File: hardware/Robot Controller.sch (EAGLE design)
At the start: 18 parts

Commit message: tighten up PCB
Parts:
- removed S1: (no value), switch-omron:10-XX
- added JP7: (no value), pinhead:PINHD-1X8
- JP8: device pinhead:PINHD-1X10 -> pinhead:PINHD-1X2
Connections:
- net GND: now also JP8.2; no longer JP8.10, S1.S1
- net N$23: now also JP7.8; no longer JP8.8
- net N$24: now also JP7.7; no longer JP8.7
- net N$25: now also JP7.6; no longer JP8.6
- net N$26: now also JP7.5; no longer JP8.5
- net N$27: now also JP7.4; no longer JP8.4
- net N$28: now also JP7.1; no longer JP8.1
- net N$29: now also JP7.2; no longer JP8.2
- net N$30: now also JP7.3; no longer JP8.3
- net N$31: now also JP8.1; no longer S1.P
- net VCC: no longer JP8.9
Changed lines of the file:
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@@
 <part name="SUPPLY4" library="SparkFun-Aesthetics" deviceset="VCC" device=""/>
 <part name="JP6" library="pinhead" deviceset="PINHD-1X3" device=""/>
-<part name="JP8" library="pinhead" deviceset="PINHD-1X10" device=""/>
-<part name="SUPPLY5" library="SparkFun-Aesthetics" deviceset="VCC" device=""/>
-<part name="GND11" library="SparkFun-Aesthetics" deviceset="GND" device=""/>
-<part name="S1" library="switch-omron" deviceset="10-XX" device=""/>
 <part name="GND12" library="SparkFun-Aesthetics" deviceset="GND" device=""/>
+<part name="JP7" library="pinhead" deviceset="PINHD-1X8" device=""/>
+<part name="JP8" library="pinhead" deviceset="PINHD-1X2" device=""/>
 </parts>
 <sheets>
@@
 <instance part="SUPPLY4" gate="1" x="121.92" y="86.36" rot="R180"/>
 <instance part="JP6" gate="A" x="38.1" y="91.44"/>
-<instance part="JP8" gate="A" x="5.08" y="104.14" rot="R90"/>
-<instance part="SUPPLY5" gate="1" x="15.24" y="96.52" rot="R180"/>
-<instance part="GND11" gate="1" x="17.78" y="91.44"/>
-<instance part="S1" gate="1" x="63.5" y="124.46" rot="R270"/>
-<instance part="GND12" gate="1" x="73.66" y="121.92" rot="R90"/>
+<instance part="GND12" gate="1" x="73.66" y="124.46" rot="R90"/>
+<instance part="JP7" gate="A" x="5.08" y="104.14" rot="R90"/>
+<instance part="JP8" gate="G$1" x="66.04" y="127" rot="R90"/>
 </instances>
 <busses>
@@
 </segment>
 <segment>
-<pinref part="JP8" gate="A" pin="10"/>
-<pinref part="GND11" gate="1" pin="GND"/>
-<wire x1="17.78" y1="101.6" x2="17.78" y2="93.98" width="0.1524" layer="91"/>
-<junction x="17.78" y="101.6"/>
-<junction x="17.78" y="93.98"/>
-</segment>
-<segment>
-<pinref part="S1" gate="1" pin="S1"/>
 <pinref part="GND12" gate="1" pin="GND"/>
-<wire x1="68.58" y1="121.92" x2="71.12" y2="121.92" width="0.1524" layer="91"/>
-<junction x="68.58" y="121.92"/>
-<junction x="71.12" y="121.92"/>
+<wire x1="66.04" y1="124.46" x2="71.12" y2="124.46" width="0.1524" layer="91"/>
+<junction x="71.12" y="124.46"/>
+<pinref part="JP8" gate="G$1" pin="2"/>
+<junction x="66.04" y="124.46"/>
 </segment>
 </net>
@@
 <junction x="121.92" y="86.36"/>
 <junction x="119.38" y="96.52"/>
-</segment>
-<segment>
-<pinref part="JP8" gate="A" pin="9"/>
-<pinref part="SUPPLY5" gate="1" pin="VCC"/>
-<wire x1="15.24" y1="101.6" x2="15.24" y2="96.52" width="0.1524" layer="91"/>
-<junction x="15.24" y="96.52"/>
-<junction x="15.24" y="101.6"/>
 </segment>
 </net>
@@
 <wire x1="12.7" y1="88.9" x2="35.56" y2="88.9" width="0.1524" layer="91"/>
 <junction x="35.56" y="88.9"/>
-<pinref part="JP8" gate="A" pin="8"/>
 <wire x1="12.7" y1="93.98" x2="12.7" y2="101.6" width="0.1524" layer="91"/>
+<pinref part="JP7" gate="A" pin="8"/>
 <junction x="12.7" y="101.6"/>
 </segment>
@@
 <wire x1="10.16" y1="86.36" x2="10.16" y2="93.98" width="0.1524" layer="91"/>
 <junction x="50.8" y="60.96"/>
-<pinref part="JP8" gate="A" pin="7"/>
 <wire x1="10.16" y1="93.98" x2="10.16" y2="101.6" width="0.1524" layer="91"/>
+<pinref part="JP7" gate="A" pin="7"/>
 <junction x="10.16" y="101.6"/>
 </segment>
@@
 <wire x1="7.62" y1="83.82" x2="7.62" y2="93.98" width="0.1524" layer="91"/>
 <junction x="50.8" y="58.42"/>
-<pinref part="JP8" gate="A" pin="6"/>
 <wire x1="7.62" y1="93.98" x2="7.62" y2="101.6" width="0.1524" layer="91"/>
+<pinref part="JP7" gate="A" pin="6"/>
 <junction x="7.62" y="101.6"/>
 </segment>
@@
 <wire x1="5.08" y1="81.28" x2="5.08" y2="93.98" width="0.1524" layer="91"/>
 <junction x="50.8" y="55.88"/>
-<pinref part="JP8" gate="A" pin="5"/>
 <wire x1="5.08" y1="93.98" x2="5.08" y2="101.6" width="0.1524" layer="91"/>
+<pinref part="JP7" gate="A" pin="5"/>
 <junction x="5.08" y="101.6"/>
 </segment>
@@
 <wire x1="2.54" y1="78.74" x2="2.54" y2="93.98" width="0.1524" layer="91"/>
 <junction x="50.8" y="53.34"/>
-<pinref part="JP8" gate="A" pin="4"/>
 <wire x1="2.54" y1="93.98" x2="2.54" y2="101.6" width="0.1524" layer="91"/>
+<pinref part="JP7" gate="A" pin="4"/>
 <junction x="2.54" y="101.6"/>
 </segment>
@@
 <wire x1="-5.08" y1="86.36" x2="-5.08" y2="93.98" width="0.1524" layer="91"/>
 <junction x="66.04" y="55.88"/>
-<pinref part="JP8" gate="A" pin="1"/>
 <wire x1="-5.08" y1="93.98" x2="-5.08" y2="101.6" width="0.1524" layer="91"/>
+<pinref part="JP7" gate="A" pin="1"/>
 <junction x="-5.08" y="101.6"/>
 </segment>
@@
 <wire x1="-2.54" y1="83.82" x2="-2.54" y2="93.98" width="0.1524" layer="91"/>
 <junction x="66.04" y="53.34"/>
-<pinref part="JP8" gate="A" pin="2"/>
 <wire x1="-2.54" y1="93.98" x2="-2.54" y2="101.6" width="0.1524" layer="91"/>
+<pinref part="JP7" gate="A" pin="2"/>
 <junction x="-2.54" y="101.6"/>
 </segment>
@@
 <wire x1="0" y1="81.28" x2="0" y2="93.98" width="0.1524" layer="91"/>
 <junction x="66.04" y="50.8"/>
-<pinref part="JP8" gate="A" pin="3"/>
 <wire x1="0" y1="93.98" x2="0" y2="101.6" width="0.1524" layer="91"/>
+<pinref part="JP7" gate="A" pin="3"/>
 <junction x="0" y="101.6"/>
 </segment>
@@
 <wire x1="45.72" y1="83.82" x2="48.26" y2="83.82" width="0.1524" layer="91"/>
 <wire x1="48.26" y1="83.82" x2="48.26" y2="124.46" width="0.1524" layer="91"/>
-<pinref part="S1" gate="1" pin="P"/>
-<wire x1="48.26" y1="124.46" x2="58.42" y2="124.46" width="0.1524" layer="91"/>
+<wire x1="48.26" y1="124.46" x2="63.5" y2="124.46" width="0.1524" layer="91"/>
 <junction x="50.8" y="73.66"/>
-<junction x="58.42" y="124.46"/>
-</segment>
-</net>
+<pinref part="JP8" gate="G$1" pin="1"/>
+<junction x="63.5" y="124.46"/>
+</segment>
+</net>

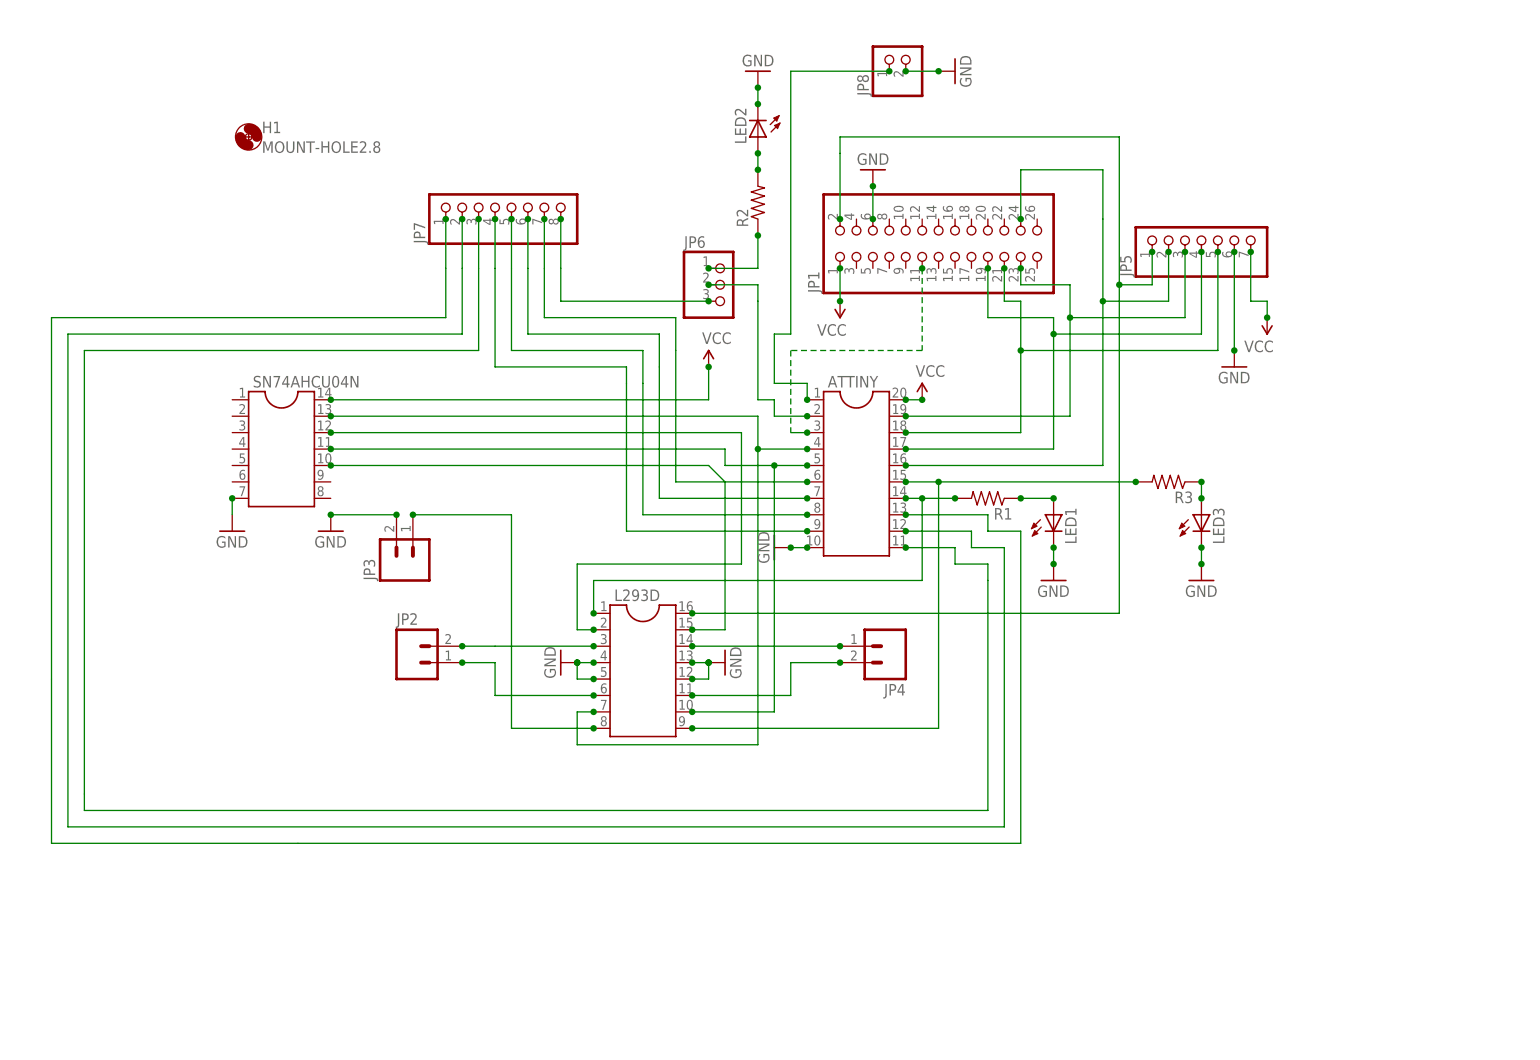
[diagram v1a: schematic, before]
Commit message: working on cleaning up schematic
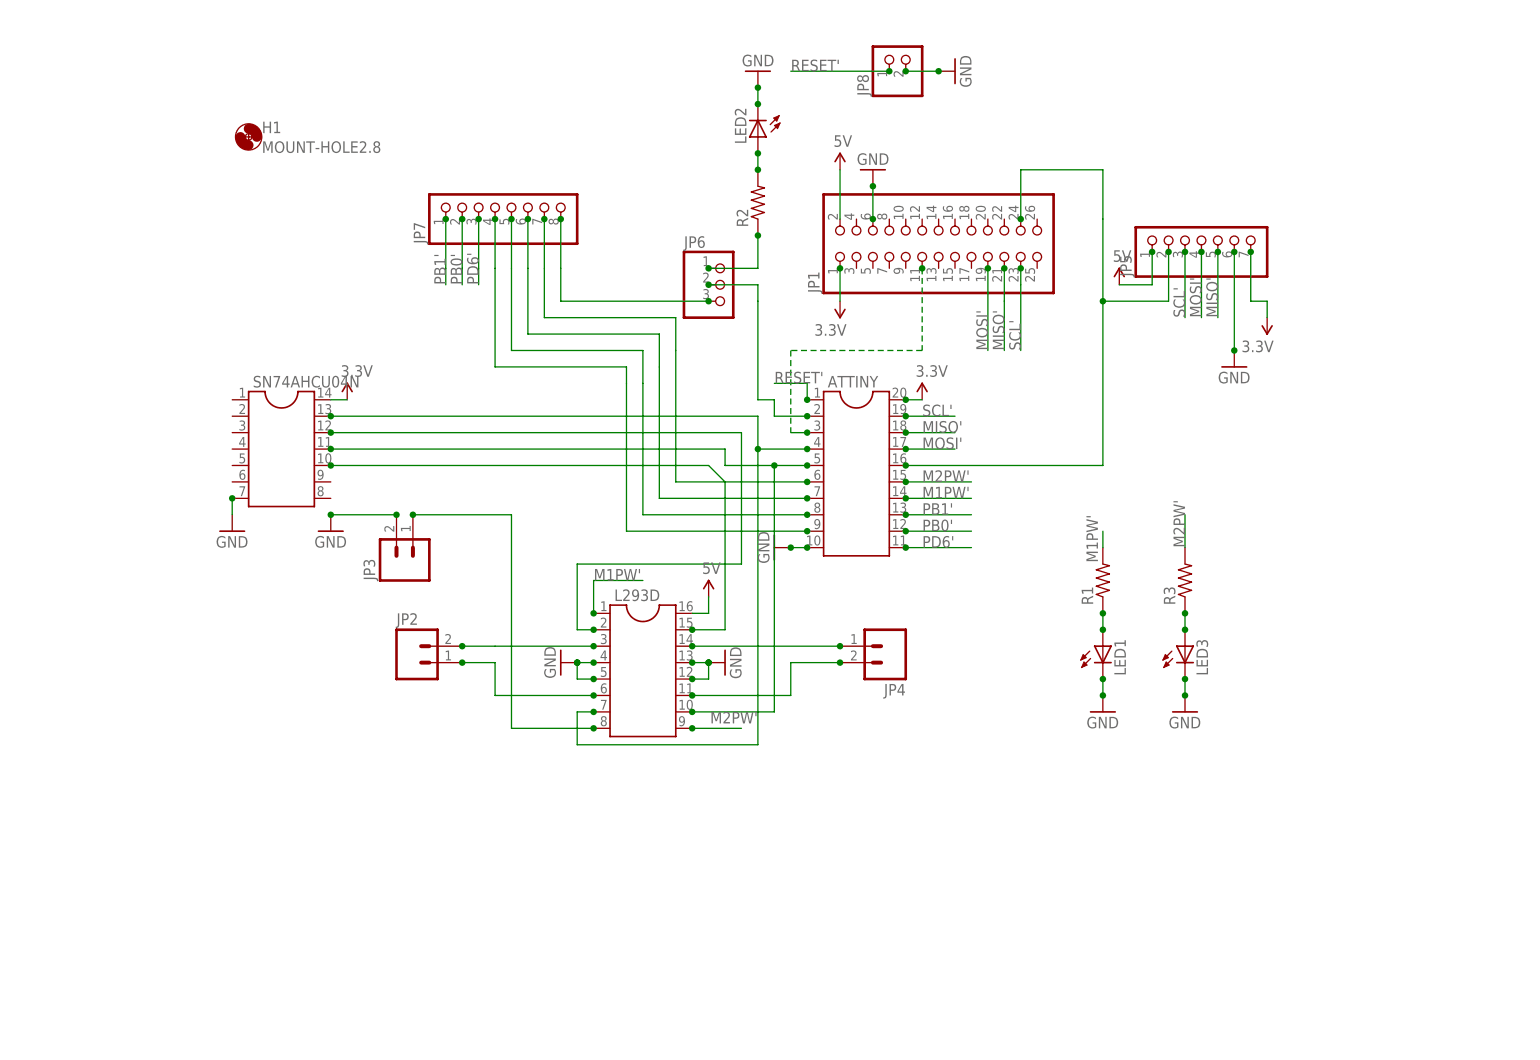
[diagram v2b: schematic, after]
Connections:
- net N$1 renamed M1PW'
- net N$11 renamed M2PW'
- net N$12 renamed 5V
- net N$28 renamed PB1'
- net N$29 renamed PB0'
- net N$30 renamed PD6'
- net N$31 renamed RESET'
- net N$5 renamed MOSI'
- net N$6 renamed MISO'
- net N$7 renamed SCL'
- net VCC renamed 3.3V
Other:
- note added: "M1PW'"
- note added: "M2PW'"
- note added: "MISO'"
- note added: "MOSI'"
- note added: "PB0'"
- note added: "PB1'"
- note added: "PD6'"
- note added: "RESET'"
- note added: "SCL'"
- moved on the sheet: LED1, LED3, R1, R3

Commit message: need ADC, upgrading to ATmega328
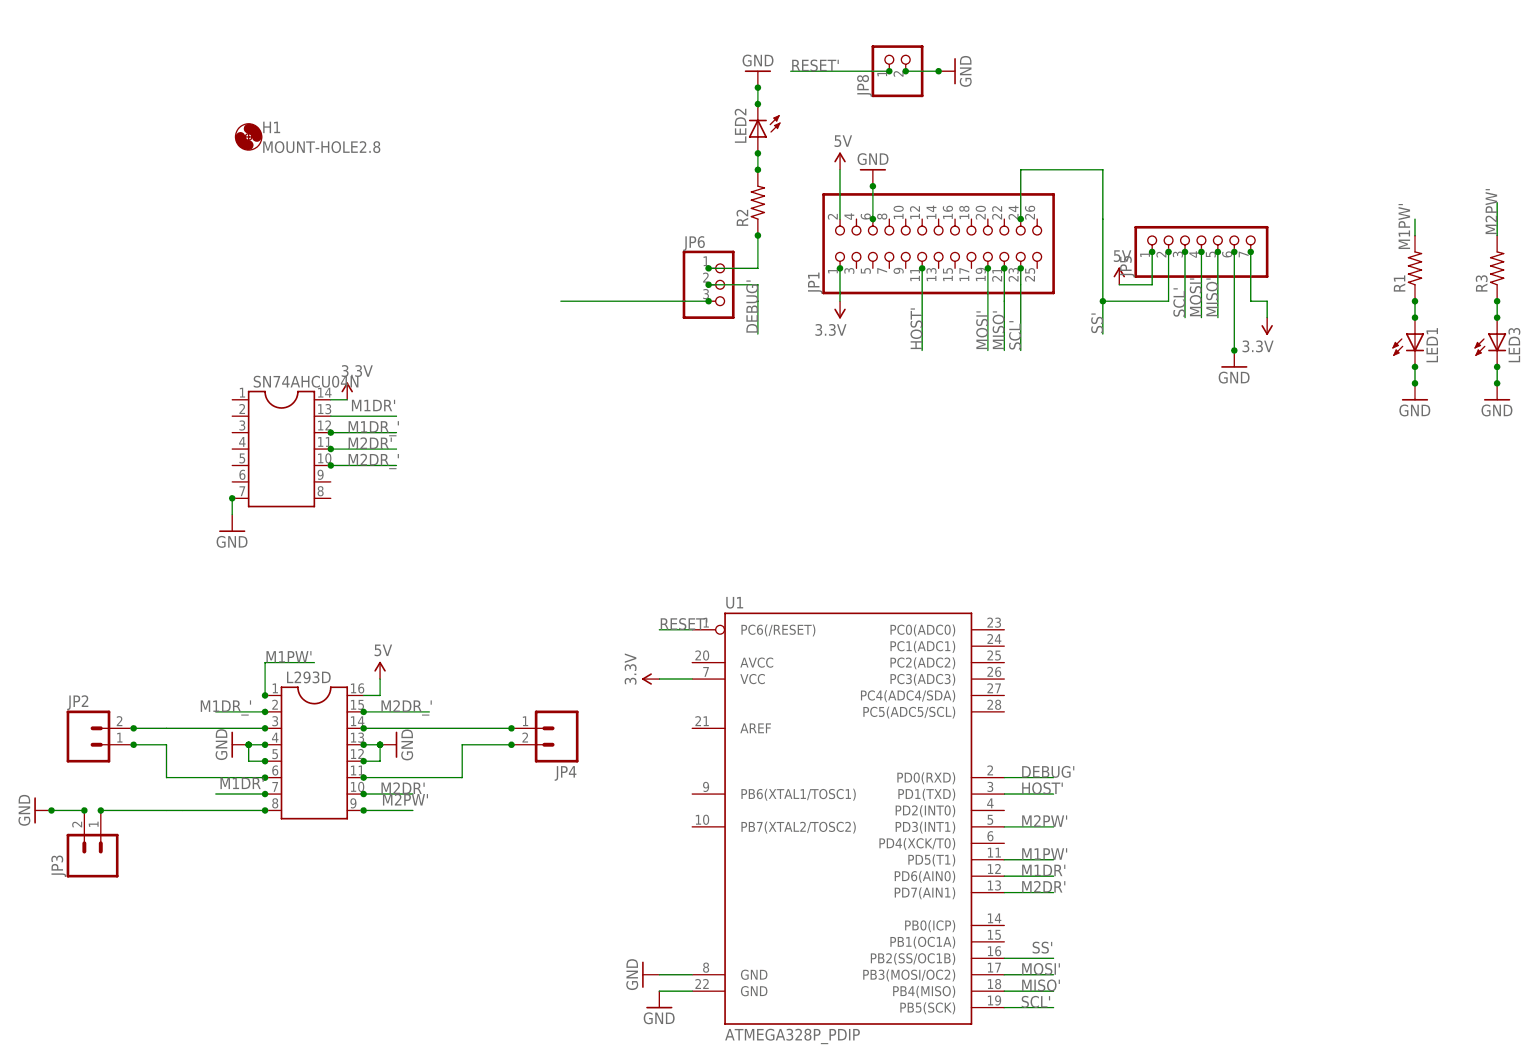
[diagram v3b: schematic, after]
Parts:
- removed ATTINY: (no value), ic-package:DIL20S
- removed JP7: (no value), pinhead:PINHD-1X8
- added U1: ATMEGA328P_PDIP, SparkFun-DigitalIC:ATMEGA328P_PDIP
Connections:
- net N$15 renamed M1DR_'
- net N$22 renamed M2DR_'
- removed net N$13: ATTINY.4, L293D.7, SN74AHCU04N.13
- removed net N$16: ATTINY.2, JP6.2
- removed net N$2: ATTINY.3, JP1.11
- removed net N$20: ATTINY.5, L293D.10, SN74AHCU04N.11
- removed net N$24: ATTINY.6, JP7.7
- removed net N$25: ATTINY.7, JP7.6
- removed net N$26: ATTINY.8, JP7.5
- removed net N$27: ATTINY.9, JP7.4
- removed net N$4: ATTINY.16, JP1.24, JP5.2
- removed net PB0': ATTINY.12, JP7.2
- removed net PB1': ATTINY.13, JP7.1
- removed net PD6': ATTINY.11, JP7.3
- new net DEBUG': JP6.2, U1.PD0(RXD)
- new net HOST': JP1.11, U1.PD1(TXD)
- new net M1DR': L293D.7, SN74AHCU04N.13, U1.PD6(AIN0)
- new net M2DR': L293D.10, SN74AHCU04N.11, U1.PD7(AIN1)
- new net SS': JP1.24, JP5.2, U1.PB2(SS/OC1B)
- net 3.3V: now also U1.VCC; no longer ATTINY.20
- net GND: now also U1.GND@1, U1.GND@2; no longer ATTINY.10
- net M1PW': now also U1.PD5(T1); no longer ATTINY.14
- net M2PW': now also U1.PD3(INT1); no longer ATTINY.15
- net MISO': now also U1.PB4(MISO); no longer ATTINY.18
- net MOSI': now also U1.PB3(MOSI/OC2); no longer ATTINY.17
- net N$23: no longer JP7.8
- net RESET': now also U1.PC6(/RESET); no longer ATTINY.1
- net SCL': now also U1.PB5(SCK); no longer ATTINY.19
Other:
- note added: "DEBUG'"
- note added: "HOST'"
- note added: "M1DR'"
- note added: "M1DR_'"
- note added: "M2DR'"
- note added: "M2DR_'"
- note added: "SS'"
- note removed: "PB0'"
- note removed: "PB1'"
- note removed: "PD6'"
- moved on the sheet: JP2, JP3, JP4, L293D, LED1, LED3, R1, R3

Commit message: WIP ATmega328 hardware
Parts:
- added JP7: (no value), pinhead:PINHD-2X13
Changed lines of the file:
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@@
 <part name="GND11" library="SparkFun-Aesthetics" deviceset="GND" device=""/>
 <part name="GND13" library="SparkFun-Aesthetics" deviceset="GND" device=""/>
+<part name="JP7" library="pinhead" deviceset="PINHD-2X13" device=""/>
 </parts>
 <sheets>
@@
 <instance part="GND11" gate="1" x="25.4" y="-15.24" rot="R270"/>
 <instance part="GND13" gate="1" x="27.94" y="-20.32"/>
+<instance part="JP7" gate="A" x="127" y="114.3" rot="R90"/>
 </instances>
 <busses>

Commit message: update connections to match todays progress
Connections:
- net M1DR': now also U1.PD2(INT0); no longer U1.PD6(AIN0)
- net M1PW': now also U1.PD6(AIN0); no longer U1.PD5(T1)
- net M2DR': now also U1.PD3(INT1); no longer U1.PD7(AIN1)
- net M2PW': no longer U1.PD3(INT1)
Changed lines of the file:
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@@
 <text x="83.82" y="-15.24" size="1.778" layer="95">MOSI'</text>
 <text x="83.82" y="-20.32" size="1.778" layer="95">SCL'</text>
-<text x="83.82" y="7.62" size="1.778" layer="95">M2PW'</text>
-<text x="83.82" y="2.54" size="1.778" layer="95">M1PW'</text>
+<text x="83.82" y="0" size="1.778" layer="95">M1PW'</text>
 <text x="83.82" y="15.24" size="1.778" layer="95">DEBUG'</text>
 <text x="83.82" y="12.7" size="1.778" layer="95">HOST'</text>
-<text x="83.82" y="0" size="1.778" layer="95">M1DR'</text>
-<text x="83.82" y="-2.54" size="1.778" layer="95">M2DR'</text>
+<text x="83.82" y="10.16" size="1.778" layer="95">M1DR'</text>
+<text x="83.82" y="7.62" size="1.778" layer="95">M2DR'</text>
 </plain>
 <instances>
@@
 </segment>
 <segment>
-<pinref part="U1" gate="G$1" pin="PD5(T1)"/>
-<wire x1="81.28" y1="2.54" x2="88.9" y2="2.54" width="0.1524" layer="91"/>
+<pinref part="U1" gate="G$1" pin="PD6(AIN0)"/>
+<wire x1="81.28" y1="0" x2="88.9" y2="0" width="0.1524" layer="91"/>
 </segment>
 </net>
@@
 <junction x="-17.78" y="10.16"/>
 </segment>
-<segment>
-<pinref part="U1" gate="G$1" pin="PD3(INT1)"/>
-<wire x1="81.28" y1="7.62" x2="88.9" y2="7.62" width="0.1524" layer="91"/>
-</segment>
 </net>
 <net name="M1DR'" class="0">
@@
 </segment>
 <segment>
-<pinref part="U1" gate="G$1" pin="PD6(AIN0)"/>
-<wire x1="81.28" y1="0" x2="88.9" y2="0" width="0.1524" layer="91"/>
+<pinref part="U1" gate="G$1" pin="PD2(INT0)"/>
+<wire x1="81.28" y1="10.16" x2="88.9" y2="10.16" width="0.1524" layer="91"/>
 </segment>
 </net>
@@
 </segment>
 <segment>
-<pinref part="U1" gate="G$1" pin="PD7(AIN1)"/>
-<wire x1="81.28" y1="-2.54" x2="88.9" y2="-2.54" width="0.1524" layer="91"/>
-</segment>
-</net>
+<pinref part="U1" gate="G$1" pin="PD3(INT1)"/>
+<wire x1="81.28" y1="7.62" x2="88.9" y2="7.62" width="0.1524" layer="91"/>
+</segment>
+</net>
